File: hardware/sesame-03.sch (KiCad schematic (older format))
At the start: 15 parts, among them IC1 ATMEGA8-P, Q1 PN2222A, SW1 SW_PUSH_SMALL_H, U1 HC-06

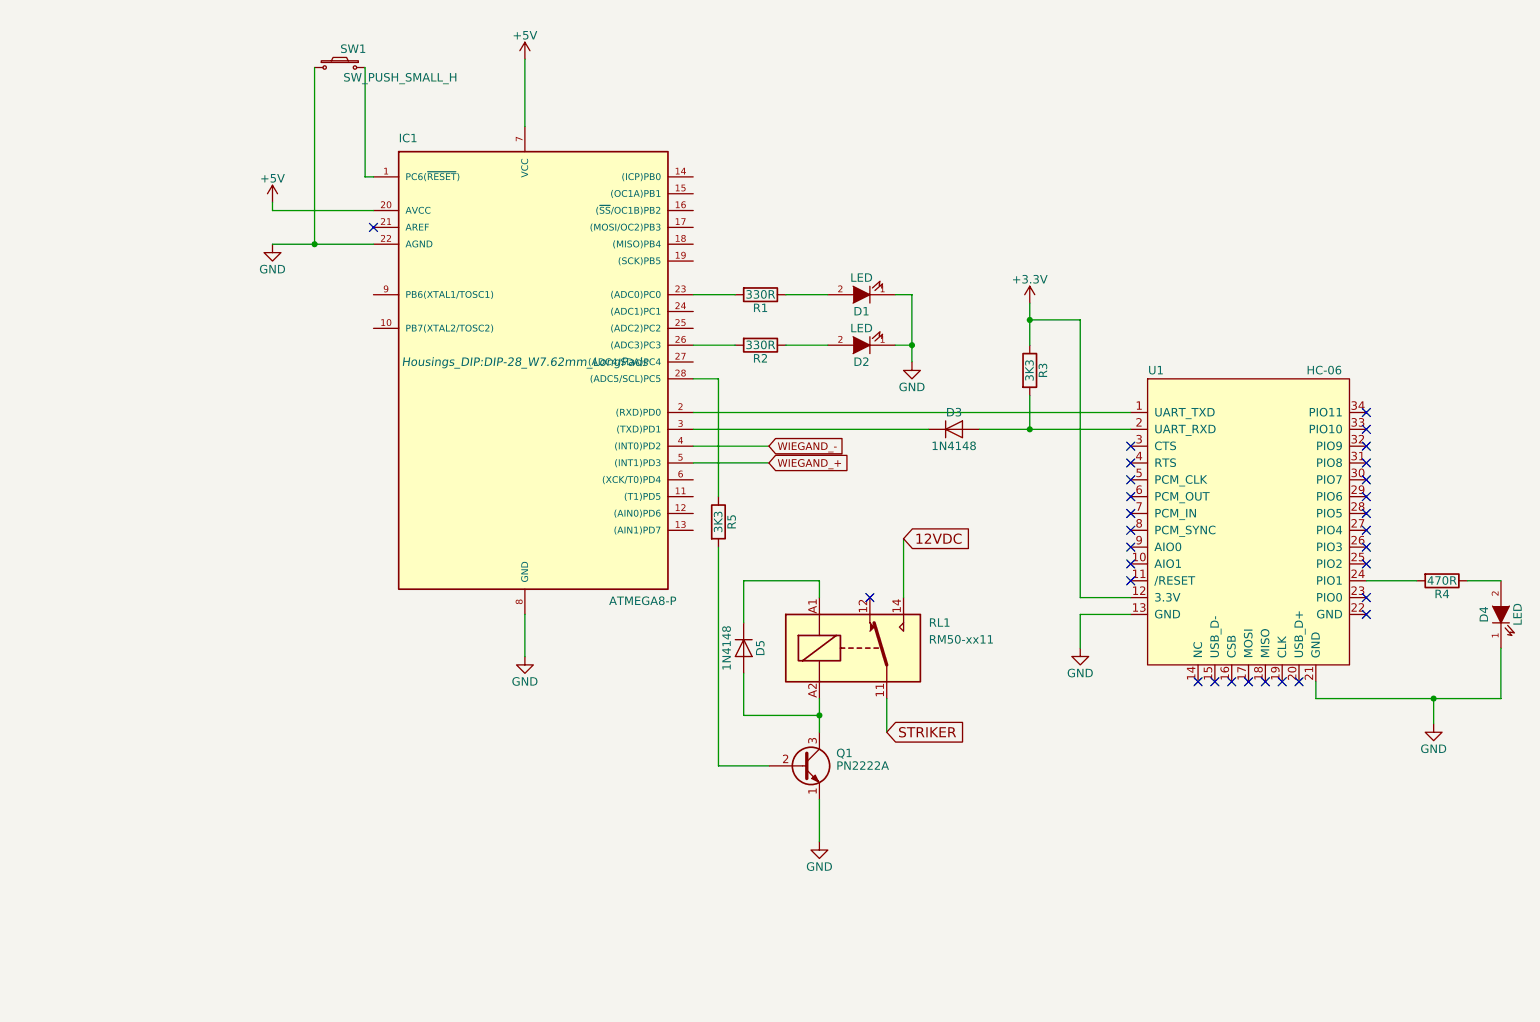
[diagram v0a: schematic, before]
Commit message: Bug#180 Add factory reset switch.
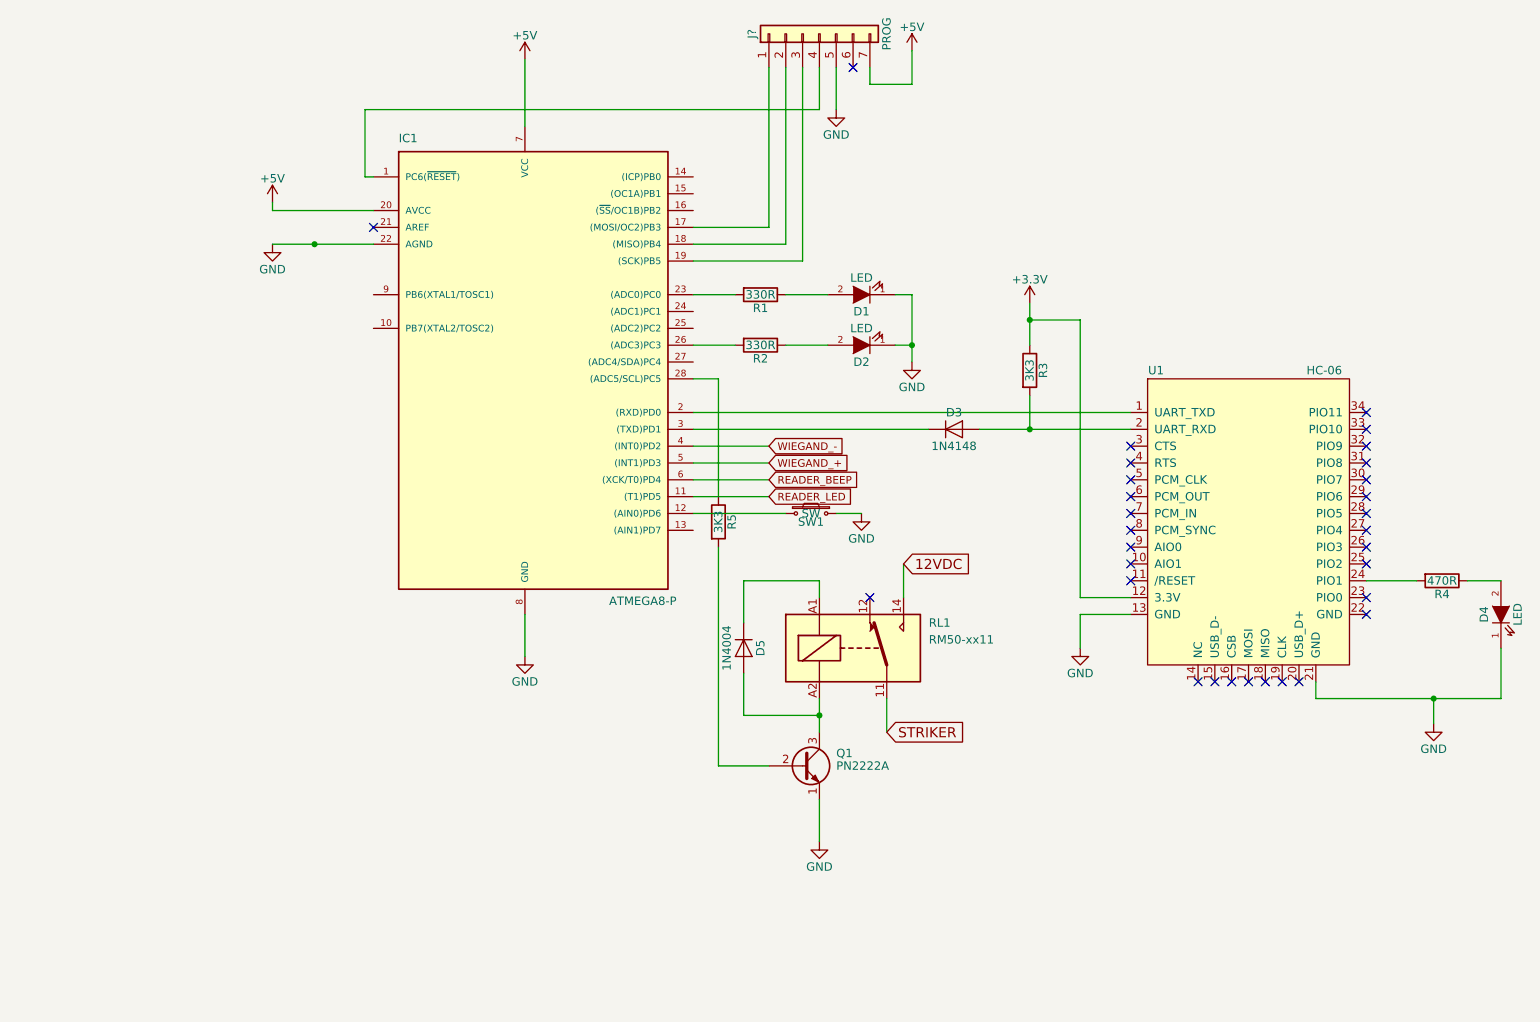
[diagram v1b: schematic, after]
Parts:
- added J?: PROG, symbol Conn_01x07
- D5: value 1N4148 -> 1N4004
- SW1: value SW_PUSH_SMALL_H -> SW
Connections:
- net +5V: now also J?.7 (Pin_7)
- net GND: now also SW1.2, J?.5 (Pin_5); no longer SW1.1
- net at IC1.1 (PC6(~RESET~)): now also J?.4 (Pin_4); no longer SW1.2
- net READER_LED: now reaches IC1.11 ((T1)PD5)
- net at IC1.12 ((AIN0)PD6): now also SW1.1
- net at IC1.17 ((MOSI/OC2)PB3): now also J?.1 (Pin_1)
- net at IC1.18 ((MISO)PB4): now also J?.2 (Pin_2)
- net at IC1.19 ((SCK)PB5): now also J?.3 (Pin_3)
- net READER_BEEP: now reaches IC1.6 ((XCK/T0)PD4)
- no-connect marks 30 -> 31
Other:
- moved on the sheet: SW1
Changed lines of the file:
@@
 F 0 "IC1" H 2950 4800 50  0000 L BNN
 F 1 "ATMEGA8-P" H 4200 2050 50  0000 L BNN
-F 2 "Housings_DIP:DIP-28_W7.62mm_LongPads" H 3700 3500 50  0000 C CIN
+F 2 "Housings_DIP:DIP-28_W7.62mm_LongPads" H 3700 3500 50  0001 C CIN
 F 3 "" H 3700 3500 50  0000 C CNN
 	1    3700 3500
@@
 	4700 3900 6100 3900
 Wire Wire Line
-	6400 3900 7300 3900
+	6400 3900 6700 3900
+Wire Wire Line
+	6700 3900 7300 3900
 Wire Wire Line
 	6700 3900 6700 3700
 Wire Wire Line
-	6700 3400 6700 3150
+	6700 3150 6700 3250
+Wire Wire Line
+	6700 3250 6700 3400
 $Comp
 L HC-06 U1
@@
 	9500 5500 9500 5200
 Wire Wire Line
-	8400 5500 9500 5500
+	8400 5500 9100 5500
+Wire Wire Line
+	9100 5500 9500 5500
 Wire Wire Line
 	9100 5500 9100 5650
@@
 	7000 5000 7000 5200
 Wire Wire Line
-	2800 2800 2200 2800
+	2200 2800 2450 2800
+Wire Wire Line
+	2450 2800 2800 2800
 Wire Wire Line
 	2800 2600 2200 2600
@@
 	5900 3100 6000 3100
 Wire Wire Line
-	6000 3100 6000 3500
+	6000 3100 6000 3400
+Wire Wire Line
+	6000 3400 6000 3500
 Wire Wire Line
 	5900 3400 6000 3400
@@
 P 5000 5200
 F 0 "D5" H 5000 5300 50  0000 C CNN
-F 1 "1N4148" H 5000 5100 50  0000 C CNN
+F 1 "1N4004" H 5000 5100 50  0000 C CNN
 F 2 "Diodes_ThroughHole:Diode_DO-35_SOD27_Horizontal_RM10" H 5000 5200 50  0001 C CNN
 F 3 "" H 5000 5200 50  0000 C CNN
@@
 	1    0    0    -1
 $EndComp
-Text GLabel 5950 4550 2    60   Input ~ 0
+Text GLabel 5950 4700 2    60   Input ~ 0
 12VDC
 Wire Wire Line
-	5950 4900 5950 4550
+	5950 4900 5950 4700
 Text GLabel 5850 5700 2    60   Input ~ 0
 STRIKER
@@
 	5850 5500 5850 5700
 Wire Wire Line
-	5450 5500 5450 5700
+	5450 5500 5450 5600
+Wire Wire Line
+	5450 5600 5450 5700
 Wire Wire Line
 	5450 4900 5450 4800
@@
 L SW_PUSH_SMALL_H SW1
 U 1 1 57A9ECAE
-P 2600 1750
-F 0 "SW1" H 2680 1860 50  0000 C CNN
-F 1 "SW_PUSH_SMALL_H" H 2960 1690 50  0000 C CNN
-F 2 "Pin_Headers:Pin_Header_Straight_1x02" H 2600 1950 50  0001 C CNN
-F 3 "" H 2600 1950 50  0000 C CNN
-	1    2600 1750
-	1    0    0    -1
-$EndComp
-Wire Wire Line
-	2750 1750 2750 2400
+P 5400 4400
+F 0 "SW1" H 5400 4350 50  0000 C CNN
+F 1 "SW" H 5400 4400 50  0000 C CNN
+F 2 "Pin_Headers:Pin_Header_Straight_1x02" H 5400 4600 50  0001 C CNN
+F 3 "" H 5400 4600 50  0000 C CNN
+	1    5400 4400
+	1    0    0    -1
+$EndComp
 Wire Wire Line
 	2750 2400 2800 2400
-Wire Wire Line
-	2450 1750 2450 2800
 Connection ~ 2450 2800
 Text GLabel 5150 4100 2    45   Input ~ 0
@@
 NoConn ~ 5750 4900
 NoConn ~ 2800 2700
+$Comp
+L Conn_01x07 J?
+U 1 1 5B1276C8
+P 5450 1550
+F 0 "J?" H 5450 1950 50  0000 C CNN
+F 1 "PROG" H 5450 1150 50  0000 C CNN
+F 2 "" H 5450 1550 50  0001 C CNN
+F 3 "" H 5450 1550 50  0001 C CNN
+	1    5450 1550
+	0    -1   -1   0
+$EndComp
+Wire Wire Line
+	4700 2700 5150 2700
+Wire Wire Line
+	5150 2700 5150 1750
+Wire Wire Line
+	4700 2800 5250 2800
+Wire Wire Line
+	5250 2800 5250 1750
+Wire Wire Line
+	4700 2900 5350 2900
+Wire Wire Line
+	5350 2900 5350 1750
+Wire Wire Line
+	2750 2000 5450 2000
+Wire Wire Line
+	5450 2000 5450 1750
+NoConn ~ 5650 1750
+$Comp
+L GND #PWR?
+U 1 1 5B127CBD
+P 5550 2000
+F 0 "#PWR?" H 5550 1750 50  0001 C CNN
+F 1 "GND" H 5550 1850 50  0000 C CNN
+F 2 "" H 5550 2000 50  0000 C CNN
+F 3 "" H 5550 2000 50  0000 C CNN
+	1    5550 2000
+	1    0    0    -1
+$EndComp
+$Comp
+L +5V #PWR?
+U 1 1 5B127D2E
+P 6000 1650
+F 0 "#PWR?" H 6000 1500 50  0001 C CNN
+F 1 "+5V" H 6000 1790 50  0000 C CNN
+F 2 "" H 6000 1650 50  0000 C CNN
+F 3 "" H 6000 1650 50  0000 C CNN
+	1    6000 1650
+	1    0    0    -1
+$EndComp
+Wire Wire Line
+	5550 2000 5550 1750
+Wire Wire Line
+	5750 1750 5750 1850
+Wire Wire Line
+	5750 1850 6000 1850
+Wire Wire Line
+	6000 1850 6000 1650
+Text GLabel 5150 4200 2    45   Input ~ 0
+READER_BEEP
+Text GLabel 5150 4300 2    45   Input ~ 0
+READER_LED
+Wire Wire Line
+	4700 4200 5150 4200
+Wire Wire Line
+	4700 4300 5150 4300
+Wire Wire Line
+	2750 2400 2750 2000
+$Comp
+L GND #PWR?
+U 1 1 5B164ABE
+P 5700 4400
+F 0 "#PWR?" H 5700 4150 50  0001 C CNN
+F 1 "GND" H 5700 4250 50  0000 C CNN
+F 2 "" H 5700 4400 50  0000 C CNN
+F 3 "" H 5700 4400 50  0000 C CNN
+	1    5700 4400
+	1    0    0    -1
+$EndComp
+Wire Wire Line
+	4700 4400 5250 4400
+Wire Wire Line
+	5550 4400 5700 4400
 $EndSCHEMATC

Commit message: Put LED colours on schematic.
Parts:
- D1: value LED -> RED; symbol LED-RESCUE-sesame-03 -> sesame-03-rescue:LED-RESCUE-sesame-03; MFR (none) -> NA; MPN (none) -> NA; SPN (none) -> NA; SPR (none) -> NA; SPURL (none) -> NA
- D2: value LED -> GREEN; symbol LED-RESCUE-sesame-03 -> sesame-03-rescue:LED-RESCUE-sesame-03; MFR (none) -> NA; MPN (none) -> NA; SPN (none) -> NA; SPR (none) -> NA; SPURL (none) -> NA
- D3, D5: symbol D -> device:D; MFR (none) -> NA; MPN (none) -> NA; SPN (none) -> NA; SPR (none) -> NA; SPURL (none) -> NA
- D4: symbol LED-RESCUE-sesame-03 -> sesame-03-rescue:LED-RESCUE-sesame-03; MFR (none) -> NA; MPN (none) -> NA; SPN (none) -> NA; SPR (none) -> NA; SPURL (none) -> NA
- IC1: symbol ATMEGA8-P -> sesame-03-rescue:ATMEGA8-P; MFR (none) -> NA; MPN (none) -> NA; SPN (none) -> NA; SPR (none) -> NA; SPURL (none) -> NA
- J?: footprint (none) -> NA; symbol Conn_01x07 -> conn:Conn_01x07
- Q1: symbol PN2222A -> transistors:PN2222A; MFR (none) -> NA; MPN (none) -> NA; SPN (none) -> NA; SPR (none) -> NA; SPURL (none) -> NA
- R1, R2, R3, R4, R5: symbol R -> device:R; MFR (none) -> NA; MPN (none) -> NA; SPN (none) -> NA; SPR (none) -> NA; SPURL (none) -> NA
- RL1: symbol RM50-xx11 -> sesame-03-rescue:RM50-xx11; MFR (none) -> NA; MPN (none) -> NA; SPN (none) -> NA; SPR (none) -> NA; SPURL (none) -> NA
- SW1: symbol SW_PUSH_SMALL_H -> sesame-03-rescue:SW_PUSH_SMALL_H; MFR (none) -> NA; MPN (none) -> NA; SPN (none) -> NA; SPR (none) -> NA; SPURL (none) -> NA
- U1: symbol HC-06 -> sesame-03-rescue:HC-06; MFR (none) -> NA; MPN (none) -> NA; SPN (none) -> NA; SPR (none) -> NA; SPURL (none) -> NA

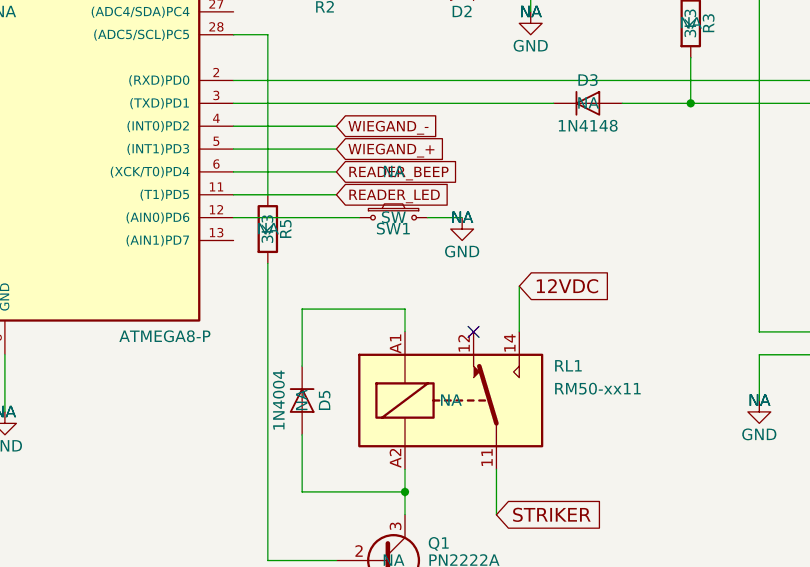
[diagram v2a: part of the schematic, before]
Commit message: Add missing +5V relay supply.
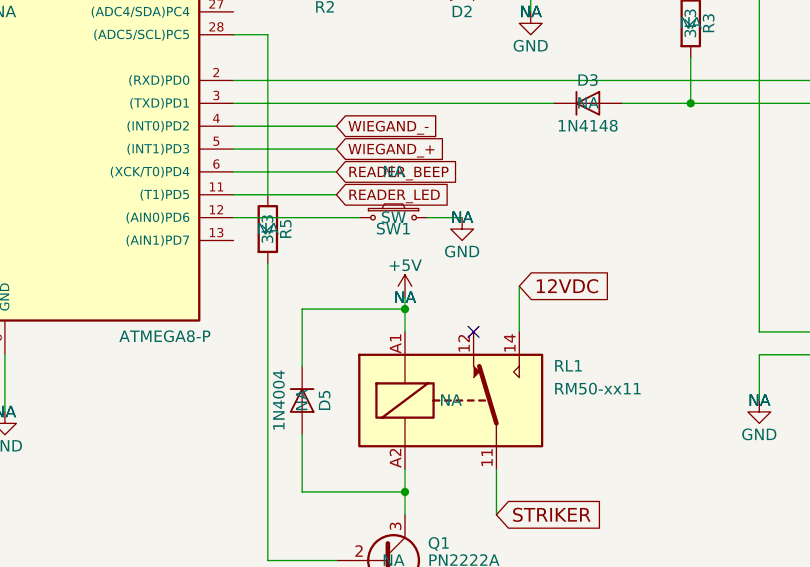
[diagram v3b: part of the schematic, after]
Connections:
- net +5V: now also D5.1 (K), RL1.A1
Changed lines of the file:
@@
 Wire Wire Line
 	2200 2800 2800 2800
+$Comp
+L power1:+5V #PWR?
+U 1 1 5CC426F8
+P 5450 4750
+F 0 "#PWR?" H 5450 4600 50  0001 C CNN
+F 1 "+5V" H 5450 4890 50  0000 C CNN
+F 2 "NA" H 5450 4750 50  0000 C CNN
+F 3 "NA" H 5450 4750 50  0000 C CNN
+	1    5450 4750
+	1    0    0    -1
+$EndComp
+Wire Wire Line
+	5450 4800 5450 4750
+Connection ~ 5450 4800
 $EndSCHEMATC

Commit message: Add missing power regulator and connector.
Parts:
- added C1, C3: CP, symbol Device:CP
- added C2: C, symbol Device:C
- added J1: Barrel_Jack, symbol Connector:Barrel_Jack
- added U2: L7805, symbol regul:L7805
- gave numbers to parts that had none: 1
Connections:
- wire segments 67 -> 85
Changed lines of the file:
@@
 $EndComp
 $Comp
-L conn:Conn_01x07 J?
+L conn:Conn_01x07 J2
 U 1 1 5B1276C8
 P 5450 1550
-F 0 "J?" H 5450 1950 50  0000 C CNN
+F 0 "J2" H 5450 1950 50  0000 C CNN
 F 1 "PROG" H 5450 1150 50  0000 C CNN
 F 2 "NA" H 5450 1550 50  0001 C CNN
@@
 $EndComp
 $Comp
-L power1:GND #PWR?
+L power1:GND #PWR012
 U 1 1 5B127CBD
 P 5550 2000
-F 0 "#PWR?" H 5550 1750 50  0001 C CNN
+F 0 "#PWR012" H 5550 1750 50  0001 C CNN
 F 1 "GND" H 5550 1850 50  0000 C CNN
 F 2 "NA" H 5550 2000 50  0000 C CNN
@@
 $EndComp
 $Comp
-L power1:+5V #PWR?
+L power1:+5V #PWR014
 U 1 1 5B127D2E
 P 6000 1650
-F 0 "#PWR?" H 6000 1500 50  0001 C CNN
+F 0 "#PWR014" H 6000 1500 50  0001 C CNN
 F 1 "+5V" H 6000 1790 50  0000 C CNN
 F 2 "NA" H 6000 1650 50  0000 C CNN
@@
 $EndComp
 $Comp
-L power1:GND #PWR?
+L power1:GND #PWR013
 U 1 1 5B164ABE
 P 5700 4400
-F 0 "#PWR?" H 5700 4150 50  0001 C CNN
+F 0 "#PWR013" H 5700 4150 50  0001 C CNN
 F 1 "GND" H 5700 4250 50  0000 C CNN
 F 2 "NA" H 5700 4400 50  0000 C CNN
@@
 	2200 2800 2800 2800
 $Comp
-L power1:+5V #PWR?
+L power1:+5V #PWR011
 U 1 1 5CC426F8
 P 5450 4750
-F 0 "#PWR?" H 5450 4600 50  0001 C CNN
+F 0 "#PWR011" H 5450 4600 50  0001 C CNN
 F 1 "+5V" H 5450 4890 50  0000 C CNN
 F 2 "NA" H 5450 4750 50  0000 C CNN
@@
 	5450 4800 5450 4750
 Connection ~ 5450 4800
+$Comp
+L regul:L7805 U2
+U 1 1 5CC44502
+P 2300 6500
+F 0 "U2" H 2150 6625 50  0000 C CNN
+F 1 "L7805" H 2300 6625 50  0000 L CNN
+F 2 "" H 2325 6350 50  0001 L CIN
+F 3 "http://www.st.com/content/ccc/resource/technical/document/datasheet/41/4f/b3/b0/12/d4/47/88/CD00000444.pdf/files/CD00000444.pdf/jcr:content/translations/en.CD00000444.pdf" H 2300 6450 50  0001 C CNN
+	1    2300 6500
+	1    0    0    -1
+$EndComp
+$Comp
+L Connector:Barrel_Jack J1
+U 1 1 5CC453B1
+P 1250 6600
+F 0 "J1" H 1250 6810 50  0000 C CNN
+F 1 "Barrel_Jack" H 1250 6400 50  0000 C CNN
+F 2 "" H 1300 6560 50  0001 C CNN
+F 3 "~" H 1300 6560 50  0001 C CNN
+	1    1250 6600
+	1    0    0    -1
+$EndComp
+$Comp
+L power1:+5V #PWR010
+U 1 1 5CC46548
+P 3150 6400
+F 0 "#PWR010" H 3150 6250 50  0001 C CNN
+F 1 "+5V" H 3150 6540 50  0000 C CNN
+F 2 "NA" H 3150 6400 50  0000 C CNN
+F 3 "NA" H 3150 6400 50  0000 C CNN
+	1    3150 6400
+	1    0    0    -1
+$EndComp
+Wire Wire Line
+	1550 6500 1800 6500
+Wire Wire Line
+	2600 6500 2700 6500
+Wire Wire Line
+	3150 6500 3150 6400
+Wire Wire Line
+	1550 6700 1550 7050
+Wire Wire Line
+	1550 7050 1800 7050
+Wire Wire Line
+	2300 7050 2300 6800
+$Comp
+L Device:CP C3
+U 1 1 5CC4B661
+P 3050 6750
+F 0 "C3" H 3075 6850 50  0000 L CNN
+F 1 "CP" H 3075 6650 50  0000 L CNN
+F 2 "" H 3088 6600 50  0001 C CNN
+F 3 "~" H 3050 6750 50  0001 C CNN
+	1    3050 6750
+	1    0    0    -1
+$EndComp
+$Comp
+L Device:C C2
+U 1 1 5CC4C00E
+P 2700 6750
+F 0 "C2" H 2725 6850 50  0000 L CNN
+F 1 "C" H 2725 6650 50  0000 L CNN
+F 2 "" H 2738 6600 50  0001 C CNN
+F 3 "~" H 2700 6750 50  0001 C CNN
+	1    2700 6750
+	1    0    0    -1
+$EndComp
+Wire Wire Line
+	2700 6600 2700 6500
+Connection ~ 2700 6500
+Wire Wire Line
+	2700 6500 3050 6500
+Wire Wire Line
+	3050 6600 3050 6500
+Connection ~ 3050 6500
+Wire Wire Line
+	3050 6500 3150 6500
+Wire Wire Line
+	2700 6900 2700 7050
+Wire Wire Line
+	2700 7050 2300 7050
+Connection ~ 2300 7050
+Wire Wire Line
+	2700 7050 3050 7050
+Wire Wire Line
+	3050 7050 3050 6900
+Connection ~ 2700 7050
+$Comp
+L Device:CP C1
+U 1 1 5CC560DF
+P 1800 6750
+F 0 "C1" H 1825 6850 50  0000 L CNN
+F 1 "CP" H 1825 6650 50  0000 L CNN
+F 2 "" H 1838 6600 50  0001 C CNN
+F 3 "~" H 1800 6750 50  0001 C CNN
+	1    1800 6750
+	1    0    0    -1
+$EndComp
+Wire Wire Line
+	1800 6600 1800 6500
+Connection ~ 1800 6500
+Wire Wire Line
+	1800 6500 2000 6500
+Wire Wire Line
+	1800 6900 1800 7050
+Connection ~ 1800 7050
+Wire Wire Line
+	1800 7050 2300 7050
 $EndSCHEMATC
